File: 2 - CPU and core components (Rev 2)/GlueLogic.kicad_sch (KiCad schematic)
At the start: 25 parts, among them J1 READ INT MODE, U1 ATF16V8B, U2 ATF22V10C, U3 ATF16V8B, U4 74HCT573, U6 74HCT374, U7 74HCT244

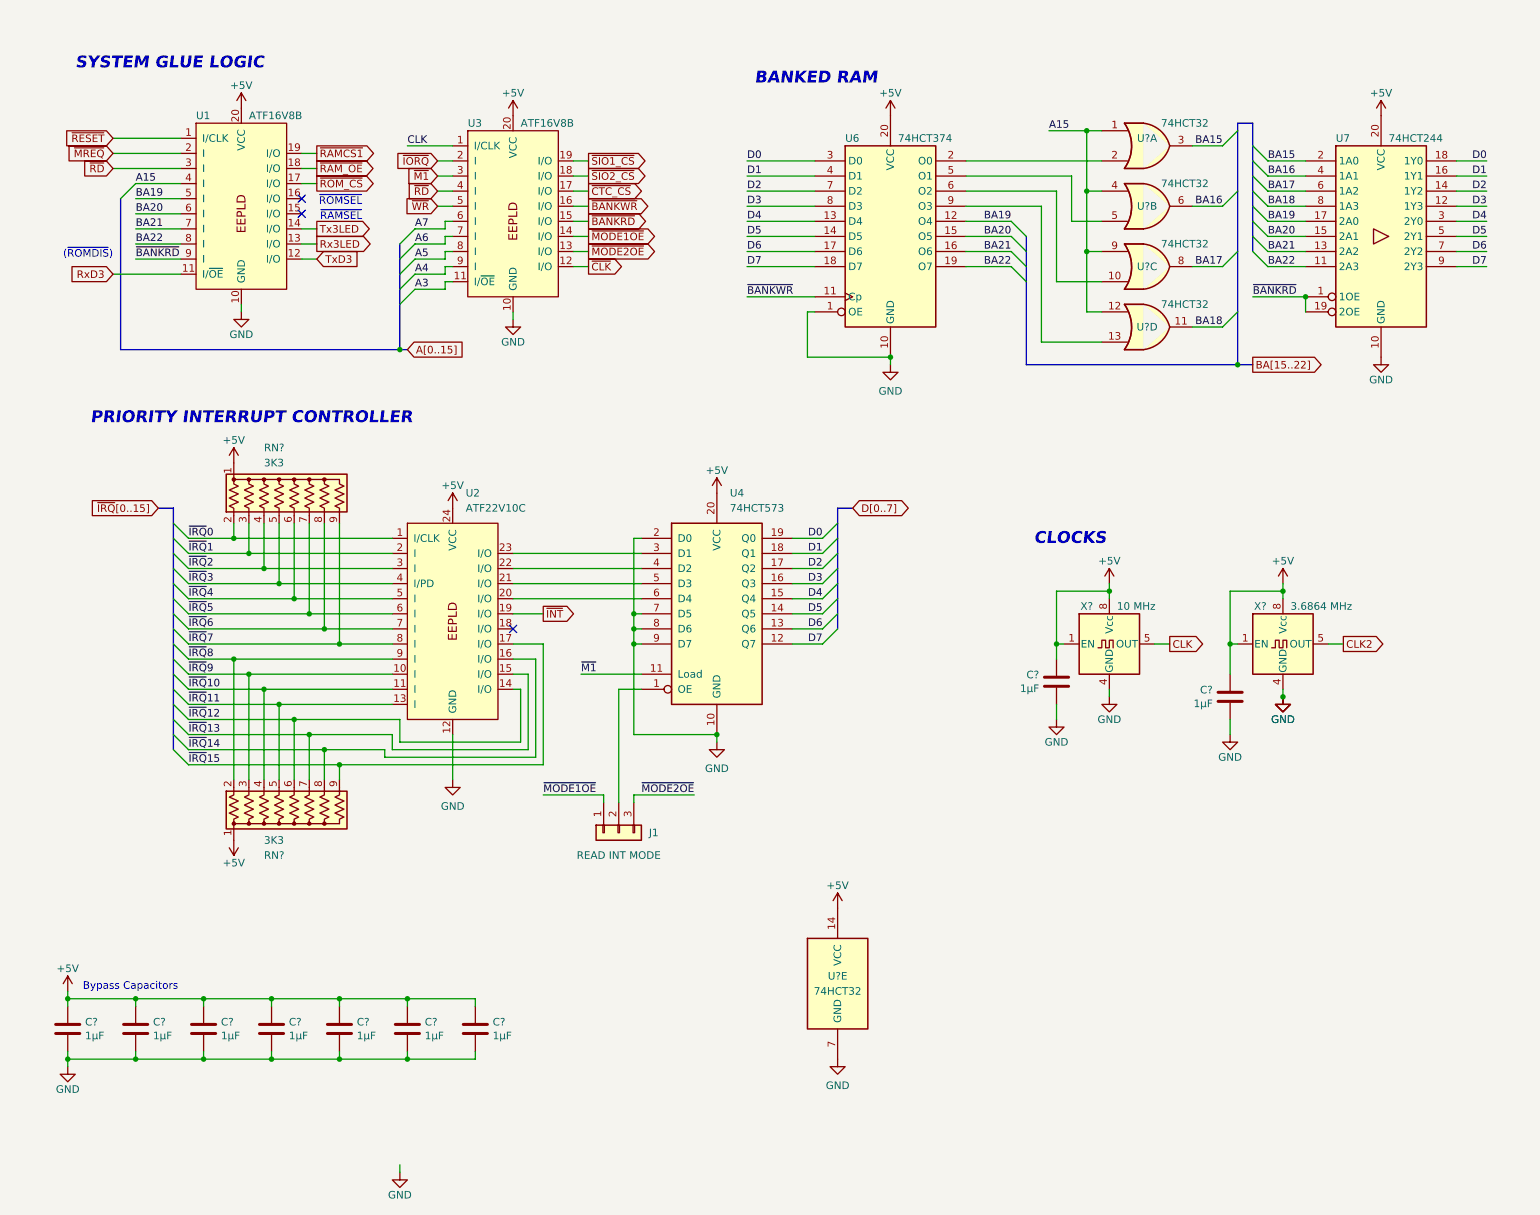
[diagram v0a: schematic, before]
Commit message: Replacing a lot of TTL chips by 2 PLDs. Also, added blinkenlights.
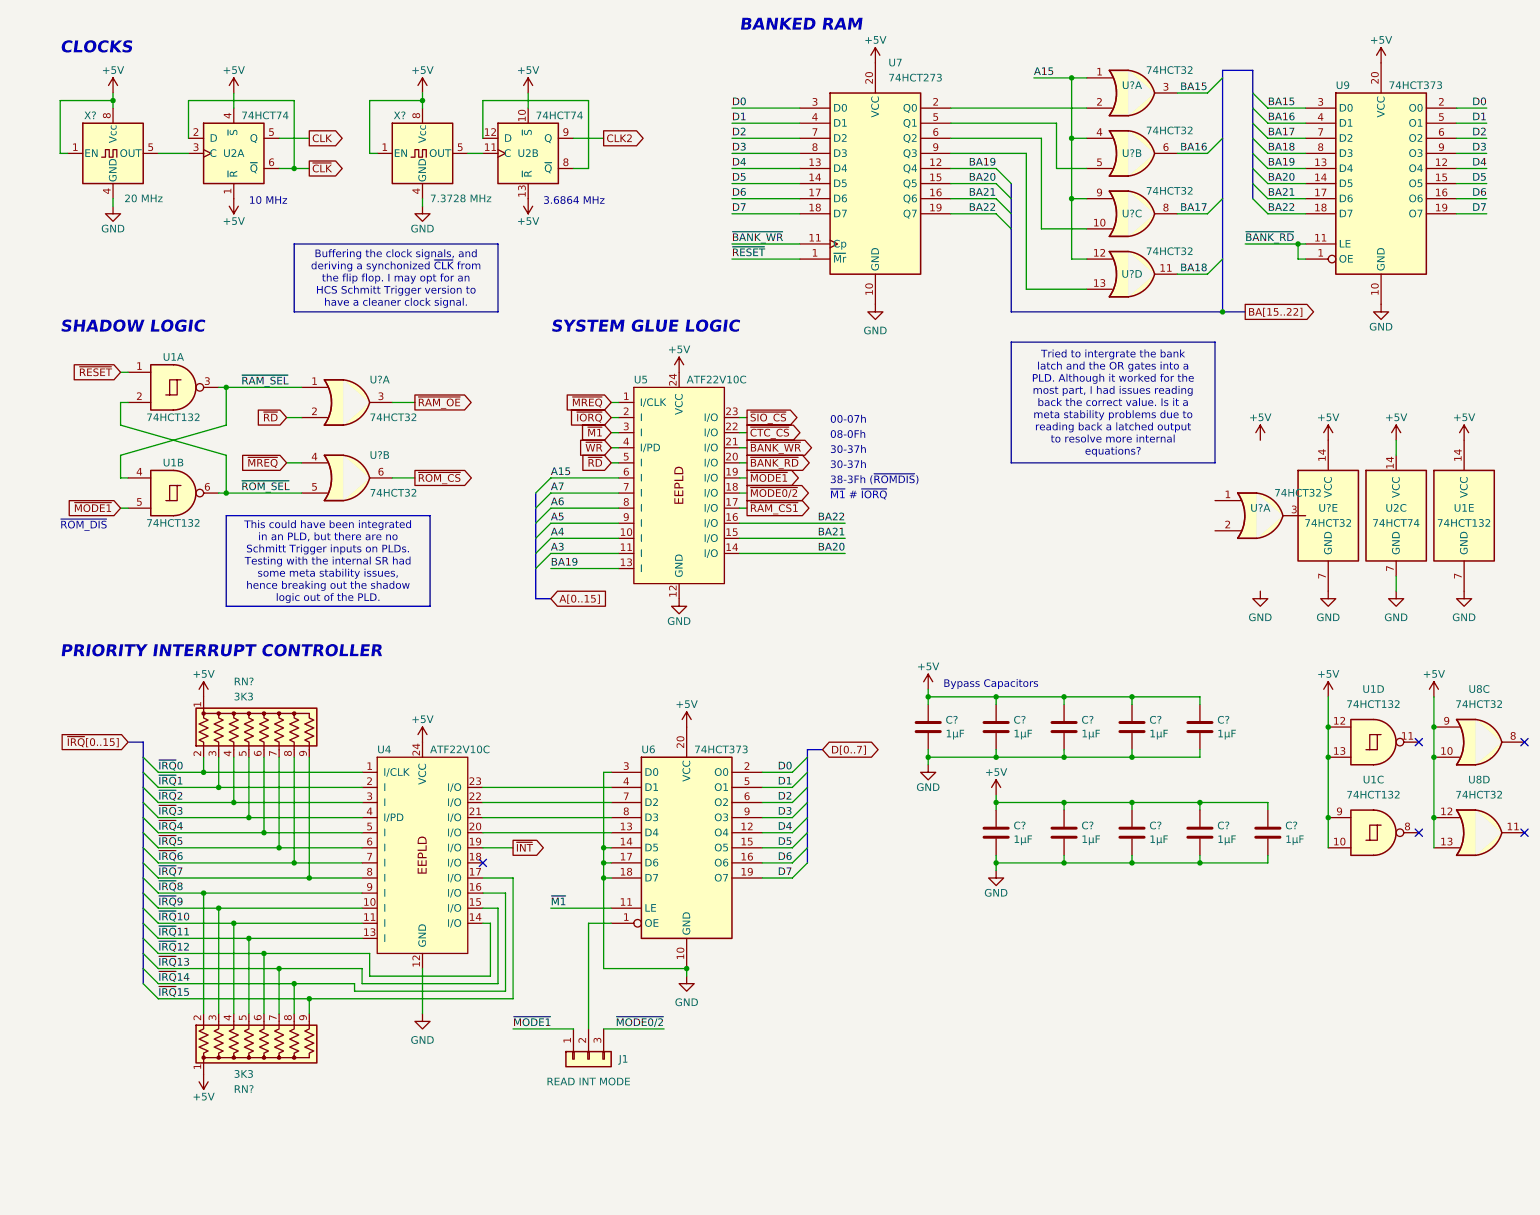
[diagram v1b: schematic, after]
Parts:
- removed C? (x9): 1µF, Capacitor_THT:C_Disc_D3.4mm_W2.1mm_P2.50mm, symbol Device:C
- removed U1, U3: ATF16V8B, Package_DIP:DIP-20_W7.62mm_Socket, symbol 0_Library:ATF16V8B
- removed U4: 74HCT573, Package_DIP:DIP-20_W7.62mm_Socket, symbol 74xx:74LS573
- removed U6: 74HCT374, Package_DIP:DIP-20_W7.62mm_Socket, symbol 74xx:74AHCT374
- removed U7: 74HCT244, Package_DIP:DIP-20_W7.62mm_Socket, symbol 74xx:74HCT244
- removed U?: 74HCT32, Package_DIP:DIP-14_W7.62mm_Socket, symbol 74xx:74LS32
- removed X?: 10 MHz, 0_Library:DIP-8-4_W7.62mm_Oscillator_Socket, symbol Oscillator:CXO_DIP8
- added C? (x5): 1µF, Capacitor_THT:C_Disc_D3.0mm_W2.0mm_P2.50mm, symbol Device:C
- added C? (x5): 1µF, Capacitor_THT:C_Disc_D3.0mm_W1.6mm_P2.50mm, symbol Device:C
- added U1: 74HCT132, Package_DIP:DIP-14_W7.62mm_Socket, symbol 74xx:74LS132
- added U2: 74HCT74, Package_DIP:DIP-14_W7.62mm_Socket, symbol 74xx:74HC74
- added U5: ATF22V10C, Package_DIP:DIP-24_W7.62mm, symbol 0_Library:ATF22V10C
- added U6, U9: 74HCT373, Package_DIP:DIP-20_W7.62mm_Socket, symbol 74xx:74LS373
- added U7: 74HCT273, Package_DIP:DIP-20_W7.62mm_Socket, symbol 74xx:74LS273
- added U8, U? (x4): 74HCT32, Package_DIP:DIP-14_W7.62mm_Socket, symbol 74xx:74LS32
- added X?: 20 MHz, 0_Library:DIP-8-4_W7.62mm_Oscillator_Socket, symbol Oscillator:CXO_DIP8
- X?: value 3.6864 MHz -> 7.3728 MHz
- renumbered U2 to U4
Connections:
- net +5V: now also C?.1, C?.1, C?.1, C?.1, C?.1, C?.1, C?.1, C?.1, C?.1, C?.1, U1.10, U1.12, U1.13, U1.14 (VCC), U1.9, U2.1 (~{R}), U2.10 (~{S}), U2.13 (~{R}), U2.14 (VCC), U2.4 (~{S}), U5.24 (VCC), U6.20 (VCC), U7.20 (VCC), U8.10, U8.12, U8.13, U8.9, U9.20 (VCC), U?.14 (VCC), X?.1 (EN), X?.8 (Vcc)
- net A15: now also U5.6 (I)
- net A3: now also U5.11 (I)
- net A4: now also U5.10 (I)
- net A5: now also U5.9 (I)
- net A6: now also U5.8 (I)
- net A7: now also U5.7 (I)
- net BA15: now also U9.3 (D0)
- net BA16: now also U9.4 (D1)
- net BA17: now also U9.7 (D2)
- net BA18: now also U9.8 (D3)
- net BA19: now also U5.13 (I), U7.12 (Q4), U9.13 (D4)
- net BA20: now also U5.14 (I/O), U7.15 (Q5), U9.14 (D5)
- net BA21: now also U5.15 (I/O), U7.16 (Q6), U9.17 (D6)
- net BA22: now also U5.16 (I/O), U7.19 (Q7), U9.18 (D7)
- net CLK: now also U2.5 (Q)
- net CLK2: now also U2.9 (Q); no longer X?.5 (OUT)
- net D0: now also U6.2 (O0), U7.3 (D0), U9.2 (O0)
- net D1: now also U6.5 (O1), U7.4 (D1), U9.5 (O1)
- net D2: now also U6.6 (O2), U7.7 (D2), U9.6 (O2)
- net D3: now also U6.9 (O3), U7.8 (D3), U9.9 (O3)
- net D4: now also U6.12 (O4), U7.13 (D4), U9.12 (O4)
- net D5: now also U6.15 (O5), U7.14 (D5), U9.15 (O5)
- net D6: now also U6.16 (O6), U7.17 (D6), U9.16 (O6)
- net D7: now also U6.19 (O7), U7.18 (D7), U9.19 (O7)
- net GND: now also C?.2, C?.2, C?.2, C?.2, C?.2, C?.2, C?.2, C?.2, C?.2, C?.2, U1.7 (GND), U2.7 (GND), U5.12 (GND), U6.10 (GND), U6.14 (D5), U6.17 (D6), U6.18 (D7), U6.3 (D0), U7.10 (GND), U9.10 (GND), U?.7 (GND), X?.4 (GND)
- net ~{CLK}: now also U2.2 (D), U2.6 (~{Q})
- net ~{CTC_CS}: now also U5.22 (I/O)
- net ~{IORQ}: now also U5.2 (I)
- net ~{M1}: now also U5.3 (I), U6.11 (LE)
- net ~{MREQ}: now also U5.1 (I/CLK), U?.4
- net ~{RAM_OE}: now also U?.3
- net ~{RD}: now also U5.5 (I), U?.2
- net ~{RESET}: now also U1.1, U7.1 (~{Mr})
- net ~{ROM_CS}: now also U?.6
- net ~{WR}: now also U5.4 (I/PD)
- net at U?.2: now also U7.2 (Q0)
- net at U?.10: now also U7.6 (Q2)
- net at J1.2 (Pin_2): now also U6.1 (OE)
- net at U4.23 (I/O): now also U6.4 (D1)
- net at U4.22 (I/O): now also U6.7 (D2)
- net at U4.21 (I/O): now also U6.8 (D3)
- net at U4.20 (I/O): now also U6.13 (D4)
- net at U?.5: now also U7.5 (Q1)
- net at U?.13: now also U7.9 (Q3)
- net ~{MODE1OE} renamed ~{MODE1}
- net ~{MODE1}: now also U1.5, U5.19 (I/O)
- net ~{MODE2OE} renamed ~{MODE0/2}
- net ~{MODE0/2}: now also U5.18 (I/O)
- new net: U2.3 (C), X?.5 (OUT)
- new net: U2.11 (C), X?.5 (OUT)
- new net: U2.12 (D), U2.8 (~{Q})
- new net ~{BANK_RD}: U5.20 (I/O), U9.1 (OE), U9.11 (LE)
- new net ~{BANK_WR}: U5.21 (I/O), U7.11 (Cp)
- new net ~{RAM_CS1}: U5.17 (I/O)
- new net ~{RAM_SEL}: U1.3, U1.4, U?.1
- new net ~{ROM_SEL}: U1.2, U1.6, U?.5
- new net ~{SIO_CS}: U5.23 (I/O)
- no-connect marks 3 -> 5
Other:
- note added: "00-07h"
- note added: "08-0Fh"
- note added: "10 MHz"
- note added: "3.6864 MHz"
- note added: "30-37h"
- note added: "38-3Fh (~{ROMDIS})"
- note added: "SHADOW LOGIC"
- note added: "~{M1} # ~{IORQ}"
- note added: "~{ROM_DIS}"
- note removed: "(~{ROMDIS})"
- note removed: "~{RAMSEL}"
- note removed: "~{ROMSEL}"
- moved on the sheet: J1, RN?, U4, U?A, U?B, U?C, U?D, X?
